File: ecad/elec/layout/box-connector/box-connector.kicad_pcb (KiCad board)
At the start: 2 copper layers, 72.5 x 12.5 mm, 4 parts

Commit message: feat(ecad): Update ecad / atopile and improve workflow
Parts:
- removed U1: , lib:BOX_EMU
- removed U2, U3: , lib:2X06_EDGE_REVERSED
- removed U4: , lib:2X02_EDGE_REVERSED
- added J1: , PWR_2X02_EDGE:2X02_EDGE_REVERSED, F.Cu at (30.0, 0.00)
- added J2: , PMOD_2X06_EDGE:2X06_EDGE_REVERSED, F.Cu at (10.0, 0.00)
- added J3: , PMOD_2X06_EDGE:2X06_EDGE_REVERSED, F.Cu at (20.0, 0.00)
- added MECH1: , BOX_EMU_OUTLINE:BOX_EMU, F.Cu at (0.00, 0.00)

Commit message: improve workflow
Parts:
- J1: moved to B.Cu
- moved J1 52.4 mm to (-22.4, -2.68)
- moved J2 17.5 mm to (-7.10, 3.67)
- moved J3 5.62 mm to (15.8, 3.68)
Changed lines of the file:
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@@
 	(footprint "PMOD_2X06_EDGE:2X06_EDGE_REVERSED"
 		(layer "F.Cu")
-		(at 10 0 0)
+		(at -7.101 3.6707 0)
 		(descr "<b>PIN HEADER</b>")
 		(property "LCSC" "DNS"
@@
 	(footprint "PMOD_2X06_EDGE:2X06_EDGE_REVERSED"
 		(layer "F.Cu")
-		(at 20 0 0)
+		(at 15.7589 3.6828 0)
 		(descr "<b>PIN HEADER</b>")
 		(property "LCSC" "DNS"
@@
 	)
 	(footprint "PWR_2X02_EDGE:2X02_EDGE_REVERSED"
-		(layer "F.Cu")
-		(at 30 0 0)
+		(layer "B.Cu")
+		(at -22.361 -2.6793 0)
 		(descr "<b>PIN HEADER</b>")
 		(property "LCSC" "DNS"
-			(at 0 0 0)
-			(layer "User.9")
-			(hide yes)
+			(at 0 -0 180)
+			(layer "User.9")
+			(hide yes)
+			(effects
+				(font
+					(size 1 1)
+					(thickness 0.2)
+				)
+				(justify mirror)
+			)
 		)
 		(property "Manufacturer" "ESP-BOX-EMU"
-			(at 0 0 0)
-			(layer "User.9")
-			(hide yes)
+			(at 0 -0 180)
+			(layer "User.9")
+			(hide yes)
+			(effects
+				(font
+					(size 1 1)
+					(thickness 0.2)
+				)
+				(justify mirror)
+			)
 		)
 		(property "Partnumber" "PWR_2X02_EDGE"
-			(at 0 0 0)
-			(layer "User.9")
-			(hide yes)
+			(at 0 -0 180)
+			(layer "User.9")
+			(hide yes)
+			(effects
+				(font
+					(size 1 1)
+					(thickness 0.2)
+				)
+				(justify mirror)
+			)
 		)
 		(property "Reference" "J1"
-			(at -2.64 -4.191 0)
-			(layer "F.SilkS")
-			(hide yes)
+			(at -2.64 4.191 180)
+			(layer "B.SilkS")
+			(hide yes)
+			(effects
+				(font
+					(size 1 1)
+					(thickness 0.2)
+				)
+				(justify mirror)
+			)
 		)
 		(property "Value" ""
-			(at 0 0 0)
-			(layer "User.9")
-			(hide yes)
+			(at 0 -0 180)
+			(layer "User.9")
+			(hide yes)
+			(effects
+				(font
+					(size 1 1)
+					(thickness 0.2)
+				)
+				(justify mirror)
+			)
 		)
 		(property "atopile_address" "pin2x2"
-			(at 0 0 0)
-			(layer "User.9")
-			(hide yes)
+			(at 0 -0 180)
+			(layer "User.9")
+			(hide yes)
+			(effects
+				(font
+					(size 1 1)
+					(thickness 0.2)
+				)
+				(justify mirror)
+			)
 		)
 		(property "lcsc_id" "DNS"
-			(at 0 0 0)
-			(layer "User.9")
-			(hide yes)
-		)
-		(fp_line
-			(start -2.54 -2.286)
-			(end -2.54 0.254)
-			(stroke
-				(width 0.1524)
-				(type solid)
-			)
-			(layer "F.SilkS")
-		)
-		(fp_line
-			(start -2.54 0.254)
-			(end 0 0.254)
-			(stroke
-				(width 0.1524)
-				(type solid)
-			)
-			(layer "F.SilkS")
-		)
-		(fp_line
-			(start -1.27 -8.636)
-			(end -1.27 -2.921)
-			(stroke
-				(width 0.762)
-				(type solid)
-			)
-			(layer "F.SilkS")
-		)
-		(fp_line
-			(start 0 -2.286)
-			(end -2.54 -2.286)
-			(stroke
-				(width 0.1524)
-				(type solid)
-			)
-			(layer "F.SilkS")
-		)
-		(fp_line
-			(start 0 0.254)
-			(end 0 -2.286)
-			(stroke
-				(width 0.1524)
-				(type solid)
-			)
-			(layer "F.SilkS")
-		)
-		(fp_line
-			(start 0 0.254)
-			(end 2.54 0.254)
-			(stroke
-				(width 0.1524)
-				(type solid)
-			)
-			(layer "F.SilkS")
-		)
-		(fp_line
-			(start 1.27 -8.636)
-			(end 1.27 -2.921)
-			(stroke
-				(width 0.762)
-				(type solid)
-			)
-			(layer "F.SilkS")
-		)
-		(fp_line
-			(start 2.54 -2.286)
-			(end 0 -2.286)
-			(stroke
-				(width 0.1524)
-				(type solid)
-			)
-			(layer "F.SilkS")
-		)
-		(fp_line
-			(start 2.54 0.254)
-			(end 2.54 -2.286)
-			(stroke
-				(width 0.1524)
-				(type solid)
-			)
-			(layer "F.SilkS")
-		)
-		(fp_poly
-			(pts
-				(xy -1.651 -2.286) (xy -0.889 -2.286) (xy -0.889 -2.794) (xy -1.651 -2.794)
-			)
-			(stroke
-				(width 0)
-				(type default)
-			)
-			(fill solid)
-			(layer "F.SilkS")
-		)
-		(fp_poly
-			(pts
-				(xy -1.651 3.27) (xy -0.889 3.27) (xy -0.889 0.254) (xy -1.651 0.254)
-			)
-			(stroke
-				(width 0)
-				(type default)
-			)
-			(fill solid)
-			(layer "F.SilkS")
-		)
-		(fp_poly
-			(pts
-				(xy 0.889 -2.286) (xy 1.651 -2.286) (xy 1.651 -2.794) (xy 0.889 -2.794)
-			)
-			(stroke
-				(width 0)
-				(type default)
-			)
-			(fill solid)
-			(layer "F.SilkS")
-		)
-		(fp_poly
-			(pts
-				(xy 0.889 3.27) (xy 1.651 3.27) (xy 1.651 0.254) (xy 0.889 0.254)
-			)
-			(stroke
-				(width 0)
-				(type default)
-			)
-			(fill solid)
-			(layer "F.SilkS")
+			(at 0 -0 180)
+			(layer "User.9")
+			(hide yes)
+			(effects
+				(font
+					(size 1 1)
+					(thickness 0.2)
+				)
+				(justify mirror)
+			)
+		)
+		(fp_line
+			(start -2.54 2.286)
+			(end -2.54 -0.254)
+			(stroke
+				(width 0.1524)
+				(type solid)
+			)
+			(layer "B.SilkS")
+		)
+		(fp_line
+			(start -2.54 -0.254)
+			(end 0 -0.254)
+			(stroke
+				(width 0.1524)
+				(type solid)
+			)
+			(layer "B.SilkS")
+		)
+		(fp_line
+			(start -1.27 8.636)
+			(end -1.27 2.921)
+			(stroke
+				(width 0.762)
+				(type solid)
+			)
+			(layer "B.SilkS")
+		)
+		(fp_line
+			(start 0 2.286)
+			(end -2.54 2.286)
+			(stroke
+				(width 0.1524)
+				(type solid)
+			)
+			(layer "B.SilkS")
+		)
+		(fp_line
+			(start 0 -0.254)
+			(end 0 2.286)
+			(stroke
+				(width 0.1524)
+				(type solid)
+			)
+			(layer "B.SilkS")
+		)
+		(fp_line
+			(start 0 -0.254)
+			(end 2.54 -0.254)
+			(stroke
+				(width 0.1524)
+				(type solid)
+			)
+			(layer "B.SilkS")
+		)
+		(fp_line
+			(start 1.27 8.636)
+			(end 1.27 2.921)
+			(stroke
+				(width 0.762)
+				(type solid)
+			)
+			(layer "B.SilkS")
+		)
+		(fp_line
+			(start 2.54 2.286)
+			(end 0 2.286)
+			(stroke
+				(width 0.1524)
+				(type solid)
+			)
+			(layer "B.SilkS")
+		)
+		(fp_line
+			(start 2.54 -0.254)
+			(end 2.54 2.286)
+			(stroke
+				(width 0.1524)
+				(type solid)
+			)
+			(layer "B.SilkS")
+		)
+		(fp_poly
+			(pts
+				(xy -1.651 2.286) (xy -0.889 2.286) (xy -0.889 2.794) (xy -1.651 2.794)
+			)
+			(stroke
+				(width 0)
+				(type default)
+			)
+			(fill solid)
+			(layer "B.SilkS")
+		)
+		(fp_poly
+			(pts
+				(xy -1.651 -3.27) (xy -0.889 -3.27) (xy -0.889 -0.254) (xy -1.651 -0.254)
+			)
+			(stroke
+				(width 0)
+				(type default)
+			)
+			(fill solid)
+			(layer "B.SilkS")
+		)
+		(fp_poly
+			(pts
+				(xy 0.889 2.286) (xy 1.651 2.286) (xy 1.651 2.794) (xy 0.889 2.794)
+			)
+			(stroke
+				(width 0)
+				(type default)
+			)
+			(fill solid)
+			(layer "B.SilkS")
+		)
+		(fp_poly
+			(pts
+				(xy 0.889 -3.27) (xy 1.651 -3.27) (xy 1.651 -0.254) (xy 0.889 -0.254)
+			)
+			(stroke
+				(width 0)
+				(type default)
+			)
+			(fill solid)
+			(layer "B.SilkS")
 		)
 		(fp_text reference "U4"
-			(at 1.778 5.969)
-			(layer "F.SilkS")
+			(at 1.778 -5.969 180)
+			(layer "B.SilkS")
 			(effects
 				(font
@@
 					(thickness 0.1143)
 				)
-				(justify left bottom)
+				(justify left bottom mirror)
 			)
 		)
 		(fp_text value ""
-			(at 4.445 3.81 90)
-			(layer "F.Fab")
+			(at 4.445 -3.81 270)
+			(layer "B.Fab")
 			(hide yes)
 			(effects
@@
 					(thickness 0.1016)
 				)
-				(justify left bottom)
+				(justify left bottom mirror)
 			)
 		)
 		(pad "1" smd rect
-			(at 1.27 2.794 90)
-			(size 3.048 1.27)
-			(layers "F.Cu" "F.Paste" "F.Mask")
+			(at 1.27 -2.794 270)
+			(size 3.048 1.27)
+			(layers "B.Cu" "B.Paste" "B.Mask")
 			(net 1 "power_5v-hv")
 			(solder_mask_margin 0.1016)
 		)
 		(pad "2" smd rect
-			(at 1.27 2.794 90)
-			(size 3.048 1.27)
-			(layers "B.Cu" "B.Paste" "B.Mask")
+			(at 1.27 -2.794 270)
+			(size 3.048 1.27)
+			(layers "F.Cu" "F.Paste" "F.Mask")
 			(net 10 "lv")
 			(solder_mask_margin 0.1016)
 		)
 		(pad "3" smd rect
-			(at -1.27 2.794 90)
-			(size 3.048 1.27)
-			(layers "F.Cu" "F.Paste" "F.Mask")
+			(at -1.27 -2.794 270)
+			(size 3.048 1.27)
+			(layers "B.Cu" "B.Paste" "B.Mask")
 			(net 10 "lv")
 			(solder_mask_margin 0.1016)
 		)
 		(pad "4" smd rect
-			(at -1.27 2.794 90)
-			(size 3.048 1.27)
-			(layers "B.Cu" "B.Paste" "B.Mask")
+			(at -1.27 -2.794 270)
+			(size 3.048 1.27)
+			(layers "F.Cu" "F.Paste" "F.Mask")
 			(net 1 "power_5v-hv")
 			(solder_mask_margin 0.1016)

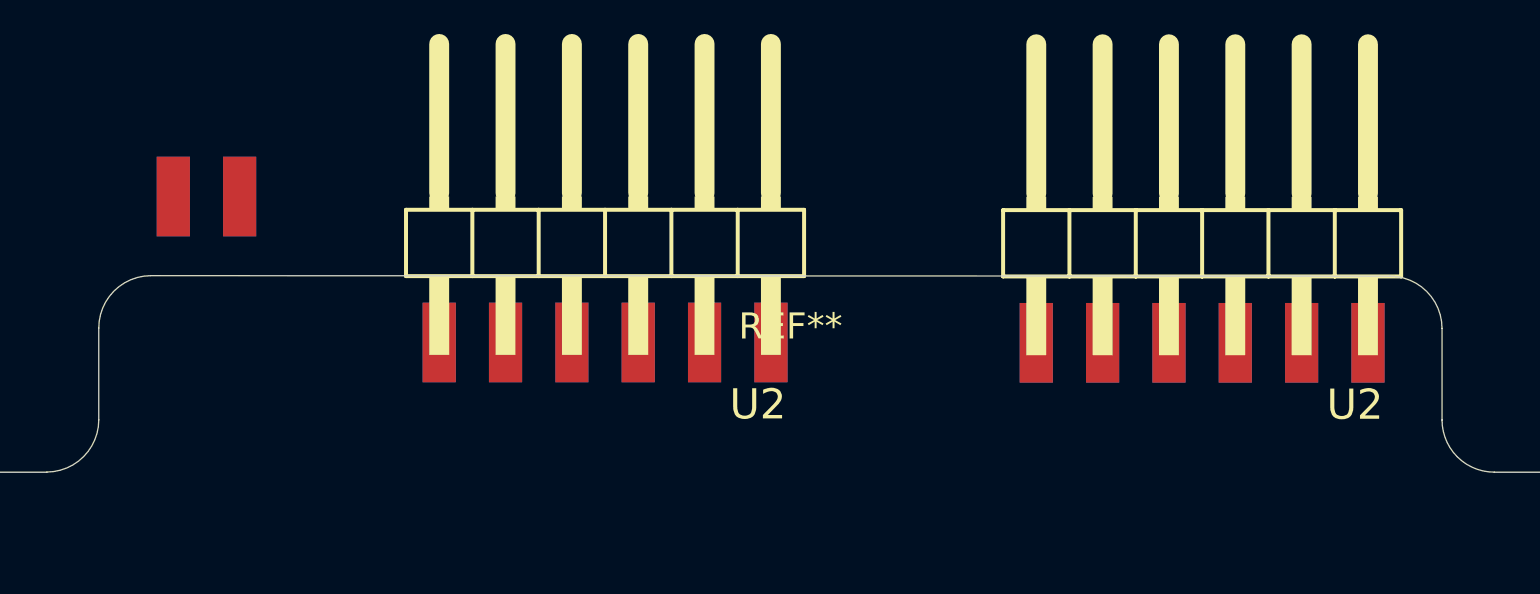
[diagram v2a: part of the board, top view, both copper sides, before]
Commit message: improve placement of components and robustness of scripts
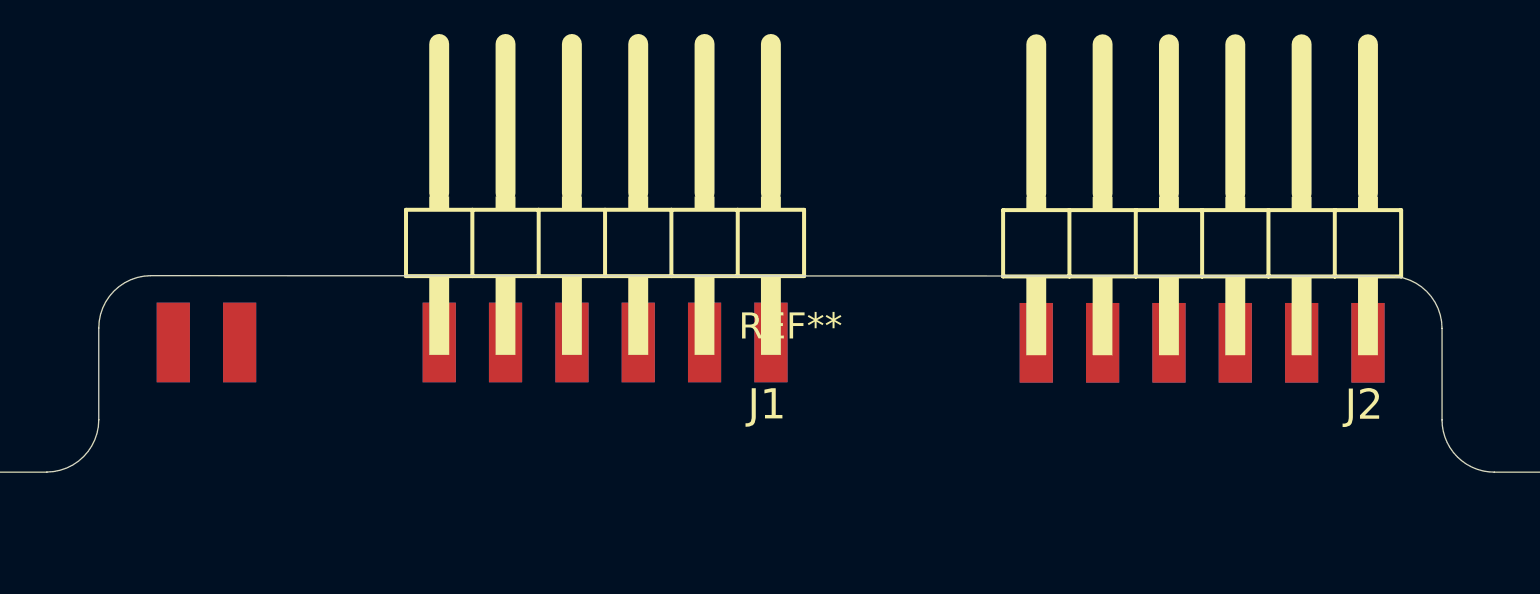
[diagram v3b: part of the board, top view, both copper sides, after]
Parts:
- turned U4 to 180 degrees
- renumbered J2 to J1, J3 to J2, MECH1 to REF**, J1 to U4
